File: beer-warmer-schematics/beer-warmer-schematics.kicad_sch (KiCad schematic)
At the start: 40 parts, among them J1 USB_C_Receptacle_6P, J2 Screw_Terminal_01x02, J3 Conn_01x07_Socket, J4 Conn_01x07_Socket, J5 Conn_01x04_Pin, J6 Screw_Terminal_01x03, Q1 AOD4184A, U2 TPS5430DDA, U3 CH224K, U4 INA219AxDCN

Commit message: routing overhaul
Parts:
- added J7, J8: Conn_01x07_Socket, Connector_PinHeader_2.54mm:PinHeader_1x07_P2.54mm_Vertical, symbol Connector_Generic:Conn_01x07
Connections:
- net +3V3: now also J7.3 (Pin_3)
- net +5V: now also J7.1 (Pin_1)
- net D0: now also J8.7 (Pin_7)
- net D1: now also J8.6 (Pin_6)
- net GND: now also J7.2 (Pin_2)
- net SCL: now also J8.2 (Pin_2)
- net SDA: now also J8.3 (Pin_3)
- net at J3.5 (Pin_5), U1.10 (D9): now also J7.5 (Pin_5)
- net at J3.4 (Pin_4), U1.11 (D10): now also J7.4 (Pin_4)
- net at J4.5 (Pin_5), U1.3 (D2): now also J8.5 (Pin_5)
- net at J4.4 (Pin_4), U1.4 (D3): now also J8.4 (Pin_4)
- net at J4.1 (Pin_1), U1.7 (D6): now also J8.1 (Pin_1)
- net at J3.7 (Pin_7), U1.8 (D7): now also J7.7 (Pin_7)
- net at J3.6 (Pin_6), U1.9 (D8): now also J7.6 (Pin_6)

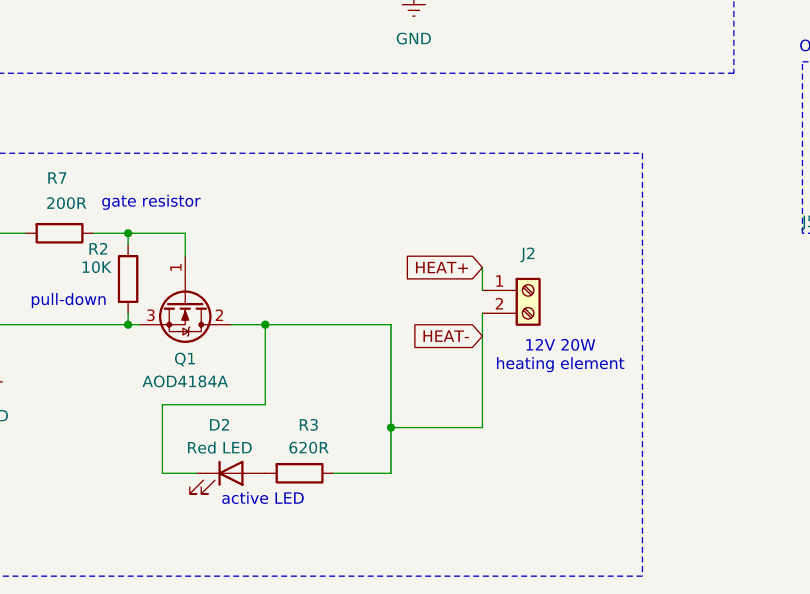
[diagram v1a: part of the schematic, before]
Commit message: active led in parallel with load
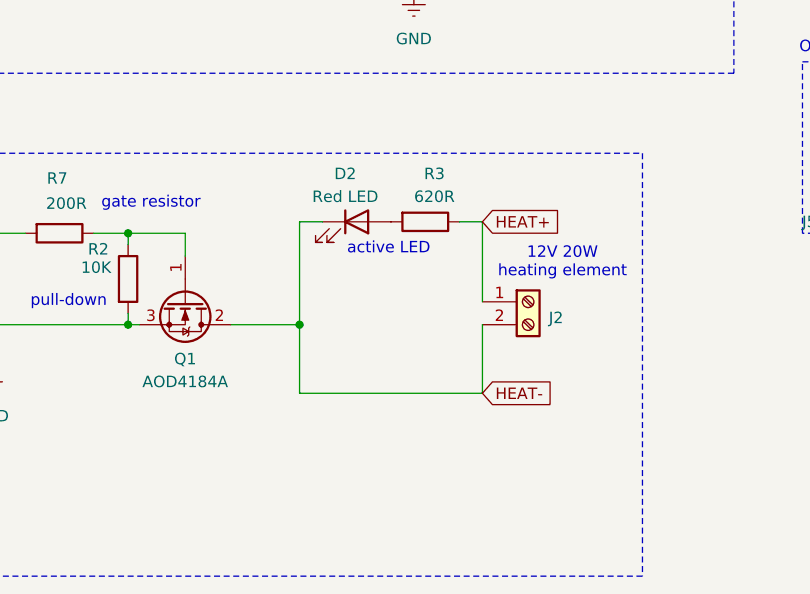
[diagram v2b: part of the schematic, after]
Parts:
- J7, J8: footprint Connector_PinHeader_2.54mm:PinHeader_1x07_P2.54mm_Vertical -> Library:PinHeader_1x07_P2.54mm_Vertical
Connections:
- net HEAT+: now also R3.1
- net HEAT-: no longer R3.1
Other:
- moved on the sheet: D2, J2, R3

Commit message: change diode on buck
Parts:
- D1: footprint Diode_SMD:D_SOD-123 -> Diode_SMD:D_SMA; LCSC C8598 -> C64982
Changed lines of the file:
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@@
 			)
 		)
-		(property "Footprint" "Diode_SMD:D_SOD-123"
+		(property "Footprint" "Diode_SMD:D_SMA"
 			(at 87.63 39.37 0)
 			(effects
@@
 			)
 		)
-		(property "LCSC" "C8598"
+		(property "LCSC" "C64982"
 			(at 87.63 39.37 90)
 			(effects

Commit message: updated with new knowledge gained
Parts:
- removed TP1: TestPoint, TestPoint:TestPoint_Pad_D1.0mm, symbol Connector:TestPoint
- added J9: Conn_01x02, Connector_PinHeader_2.54mm:PinHeader_1x02_P2.54mm_Vertical, symbol Connector_Generic:Conn_01x02
- R3: value 620R -> 200R; footprint Resistor_SMD:R_1206_3216Metric -> Resistor_SMD:R_0603_1608Metric; LCSC C25391 -> C22962
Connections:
- net GND: now also D2.1 (K), J9.2 (Pin_2)
- net HEAT+: no longer R3.1
- net VBUS: now also J9.1 (Pin_1)
- net at D2.2 (A): now also R3.1; no longer R3.2
- net at J4.4 (Pin_4), J8.4 (Pin_4), U1.4 (D3): no longer names the net of J4.4 (Pin_4), J8.4 (Pin_4), U1.4 (D3)
- net LED_OUT: now reaches J4.5 (Pin_5), J8.5 (Pin_5), U1.3 (D2)
- net LED_OUT: now also R3.2
- net +3V3 renamed +3.3V
- net D0 renamed TEMP_PROBE
- net D1 renamed HEAT_OUT
- net HEAT-: no longer names the net of J2.2 (Pin_2), Q1.2 (D)
- net HEAT-: no longer D2.1 (K)
- net VDD: no longer names the net of C6.2, R1.2, U3.1 (VDD), U3.3 (CFG3)
- no-connect marks 10 -> 3
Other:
- moved on the sheet: D2, J2, R8, R9

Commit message: production
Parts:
- added FID4, FID5, FID6: Fiducial, Fiducial:Fiducial_0.5mm_Mask1.5mm, symbol Mechanical:Fiducial
- C7: LCSC C57112 -> C1524
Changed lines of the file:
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@@
 	)
 	(symbol
+		(lib_id "Mechanical:Fiducial")
+		(at 271.78 29.21 0)
+		(unit 1)
+		(exclude_from_sim no)
+		(in_bom no)
+		(on_board yes)
+		(dnp no)
+		(fields_autoplaced yes)
+		(property "Reference" "FID5"
+			(at 274.32 27.9399 0)
+			(effects
+				(font
+					(size 1.27 1.27)
+				)
+				(justify left)
+			)
+		)
+		(property "Value" "Fiducial"
+			(at 274.32 30.4799 0)
+			(effects
+				(font
+					(size 1.27 1.27)
+				)
+				(justify left)
+			)
+		)
+		(property "Footprint" "Fiducial:Fiducial_0.5mm_Mask1.5mm"
+			(at 271.78 29.21 0)
+			(effects
+				(font
+					(size 1.27 1.27)
+				)
+				(hide yes)
+			)
+		)
+		(property "Datasheet" "~"
+			(at 271.78 29.21 0)
+			(effects
+				(font
+					(size 1.27 1.27)
+				)
+				(hide yes)
+			)
+		)
+		(property "Description" "Fiducial Marker"
+			(at 271.78 29.21 0)
+			(effects
+				(font
+					(size 1.27 1.27)
+				)
+				(hide yes)
+			)
+		)
+		(instances
+			(project "beer-warmer-schematics"
+				(path "/70572ac2-8723-48b8-abb1-12d225a3bb68"
+					(reference "FID5")
+					(unit 1)
+				)
+			)
+		)
+	)
+	(symbol
 		(lib_id "power:+5V")
 		(at 109.22 35.56 0)
@@
 	)
 	(symbol
+		(lib_id "Mechanical:Fiducial")
+		(at 271.78 24.13 0)
+		(unit 1)
+		(exclude_from_sim no)
+		(in_bom no)
+		(on_board yes)
+		(dnp no)
+		(fields_autoplaced yes)
+		(property "Reference" "FID4"
+			(at 274.32 22.8599 0)
+			(effects
+				(font
+					(size 1.27 1.27)
+				)
+				(justify left)
+			)
+		)
+		(property "Value" "Fiducial"
+			(at 274.32 25.3999 0)
+			(effects
+				(font
+					(size 1.27 1.27)
+				)
+				(justify left)
+			)
+		)
+		(property "Footprint" "Fiducial:Fiducial_0.5mm_Mask1.5mm"
+			(at 271.78 24.13 0)
+			(effects
+				(font
+					(size 1.27 1.27)
+				)
+				(hide yes)
+			)
+		)
+		(property "Datasheet" "~"
+			(at 271.78 24.13 0)
+			(effects
+				(font
+					(size 1.27 1.27)
+				)
+				(hide yes)
+			)
+		)
+		(property "Description" "Fiducial Marker"
+			(at 271.78 24.13 0)
+			(effects
+				(font
+					(size 1.27 1.27)
+				)
+				(hide yes)
+			)
+		)
+		(instances
+			(project "beer-warmer-schematics"
+				(path "/70572ac2-8723-48b8-abb1-12d225a3bb68"
+					(reference "FID4")
+					(unit 1)
+				)
+			)
+		)
+	)
+	(symbol
 		(lib_id "New_Library:Seed_Studio_Xiao_ESP32C6")
 		(at 185.42 53.34 0)
@@
 	)
 	(symbol
+		(lib_id "Mechanical:Fiducial")
+		(at 271.78 34.29 0)
+		(unit 1)
+		(exclude_from_sim no)
+		(in_bom no)
+		(on_board yes)
+		(dnp no)
+		(fields_autoplaced yes)
+		(property "Reference" "FID6"
+			(at 274.32 33.0199 0)
+			(effects
+				(font
+					(size 1.27 1.27)
+				)
+				(justify left)
+			)
+		)
+		(property "Value" "Fiducial"
+			(at 274.32 35.5599 0)
+			(effects
+				(font
+					(size 1.27 1.27)
+				)
+				(justify left)
+			)
+		)
+		(property "Footprint" "Fiducial:Fiducial_0.5mm_Mask1.5mm"
+			(at 271.78 34.29 0)
+			(effects
+				(font
+					(size 1.27 1.27)
+				)
+				(hide yes)
+			)
+		)
+		(property "Datasheet" "~"
+			(at 271.78 34.29 0)
+			(effects
+				(font
+					(size 1.27 1.27)
+				)
+				(hide yes)
+			)
+		)
+		(property "Description" "Fiducial Marker"
+			(at 271.78 34.29 0)
+			(effects
+				(font
+					(size 1.27 1.27)
+				)
+				(hide yes)
+			)
+		)
+		(instances
+			(project "beer-warmer-schematics"
+				(path "/70572ac2-8723-48b8-abb1-12d225a3bb68"
+					(reference "FID6")
+					(unit 1)
+				)
+			)
+		)
+	)
+	(symbol
 		(lib_id "Connector:Screw_Terminal_01x03")
 		(at 140.97 120.65 180)
@@
 			)
 		)
-		(property "LCSC" "C57112"
+		(property "LCSC" "C1524"
 			(at 82.55 39.37 0)
 			(effects

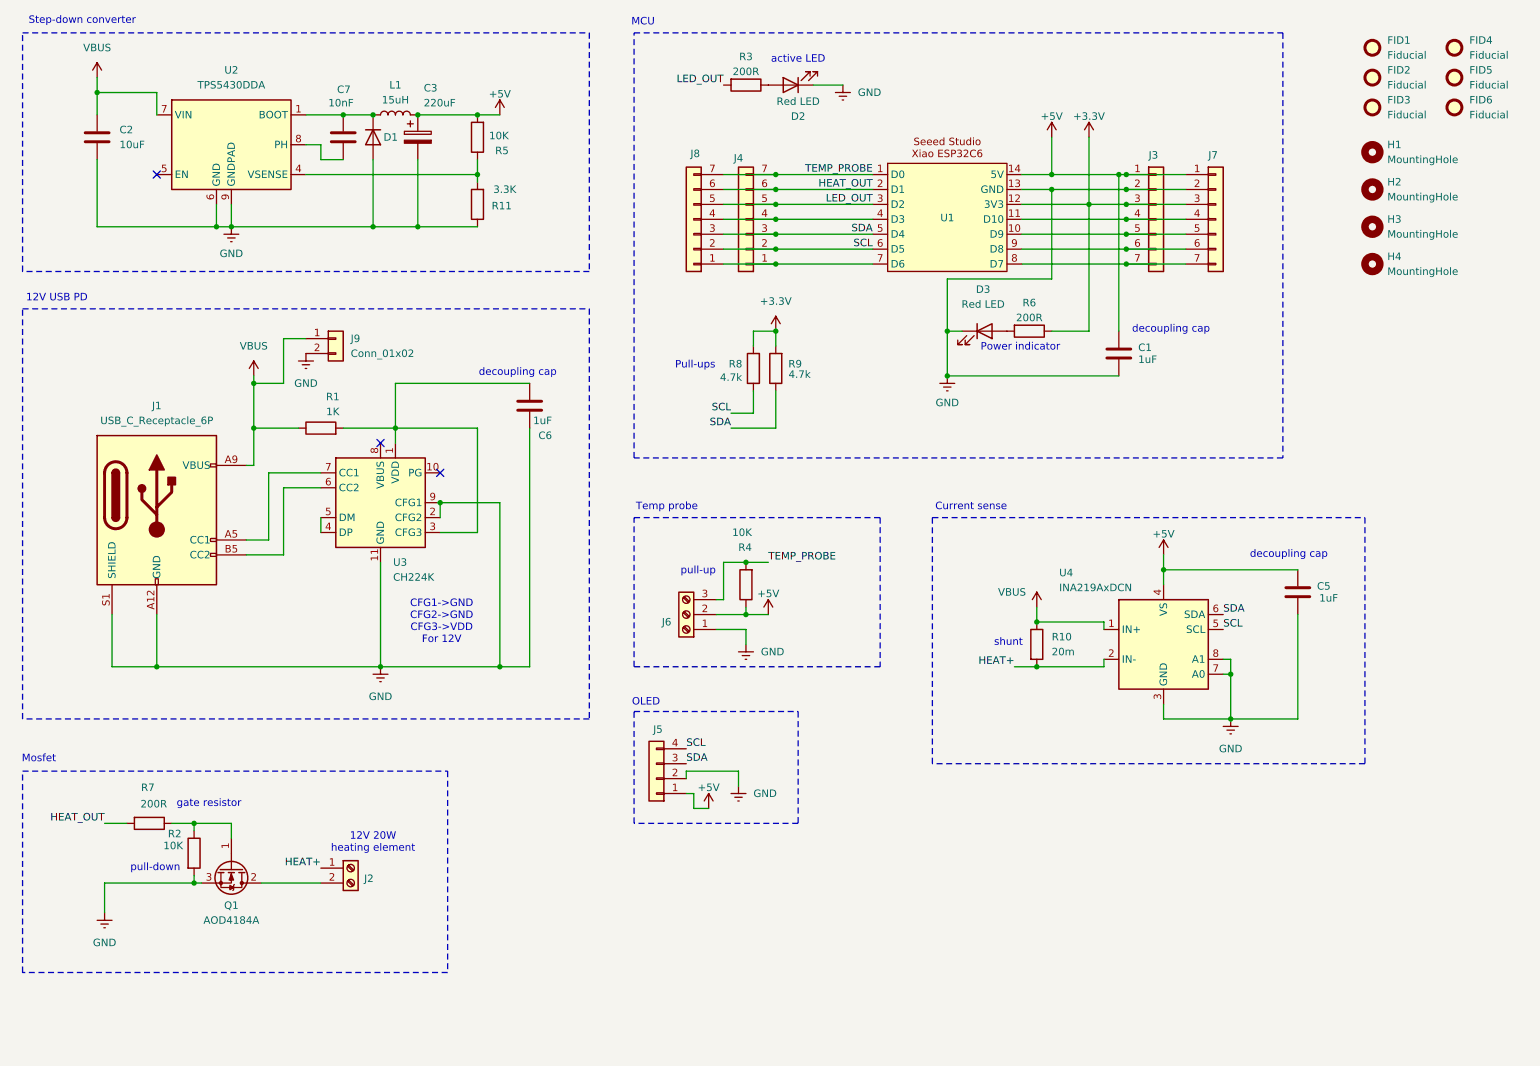
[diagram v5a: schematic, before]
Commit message: updated with learnings after production
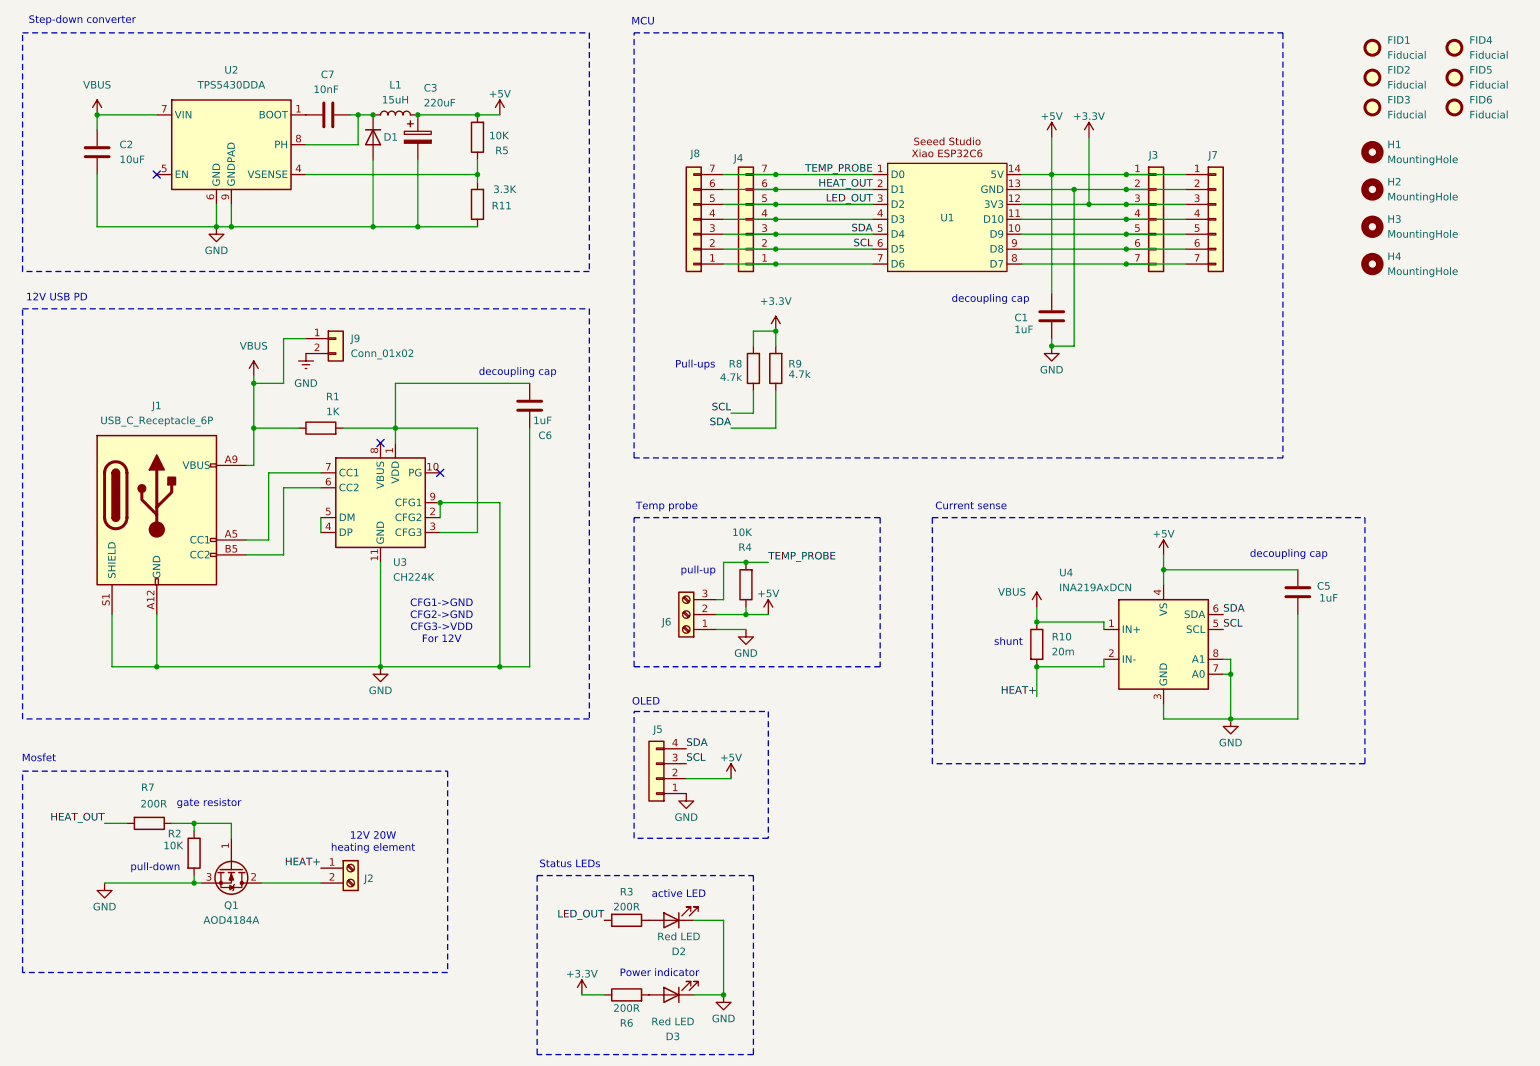
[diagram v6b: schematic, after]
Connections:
- net +5V: now also J5.2 (Pin_2); no longer J5.1 (Pin_1)
- net GND: now also J5.1 (Pin_1); no longer J5.2 (Pin_2)
- net SCL: now also J5.3 (Pin_3); no longer J5.4 (Pin_4)
- net SDA: now also J5.4 (Pin_4); no longer J5.3 (Pin_3)
- net at D1.1 (K), L1.1: now also C7.1, U2.8 (PH); no longer C7.2, U2.1 (BOOT)
- new net: C7.2, U2.1 (BOOT)
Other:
- note added: "Status LEDs"
- moved on the sheet: C1, C2, C7, D2, D3, R3, R6

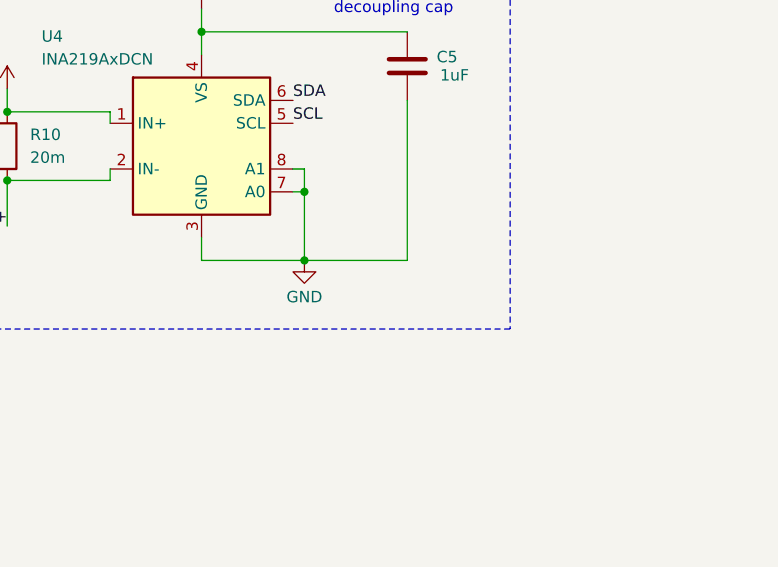
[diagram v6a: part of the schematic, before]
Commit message: current sense working, oled disabled
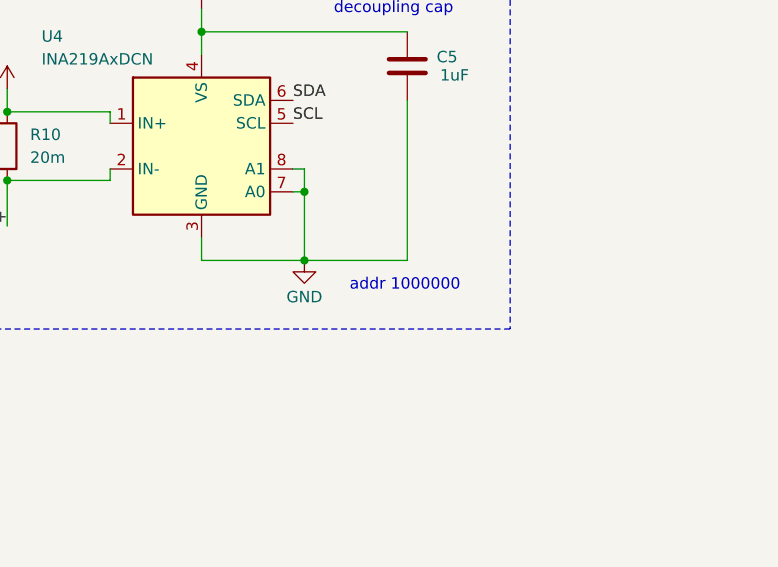
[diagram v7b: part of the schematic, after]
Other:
- note added: "addr 1000000"
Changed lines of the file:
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@@
+		)
+	)
+	(text "addr 1000000"
+		(exclude_from_sim no)
+		(at 244.856 141.224 0)
+		(effects
+			(font
+				(size 1.27 1.27)
+			)
 		)
 	)
